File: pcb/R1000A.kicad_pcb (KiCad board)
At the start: 2 copper layers, 106 x 104 mm, 21 parts, among them J1 PCIESOCKET-X1, J10 PCIESOCKET-X1, J11 PCIESOCKET-X1, J12 PCIESOCKET-X1, J13 PCIESOCKET-X1, J14 PCIESOCKET-X1, J2 PCIESOCKET-X1, J3 PCIESOCKET-X1, J4 PCIESOCKET-X1, J5 PCIESOCKET-X1, J6 PCIESOCKET-X1, J7 PCIESOCKET-X1, J8 PCIESOCKET-X1, J9 PCIESOCKET-X1

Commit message: wip
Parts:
- added MP1: RPi_Mount, Main:DOCK_RPI, F.Cu at (102.5, 68.0)
- added U1: LPC1769FBD100,551, Main:QFP050P1400X1400X160-100, F.Cu at (98.8, 68.1)
- J10, J12, J14, J2, J4, J6, J8: moved to F.Cu
- moved J1 51.0 mm to (70.0, 120.0)
- moved J10 51.0 mm to (160.0, 120.0)
- moved J11 51.0 mm to (170.0, 120.0)
- moved J12 51.0 mm to (180.0, 120.0)
- moved J13 51.0 mm to (190.0, 120.0)
- moved J14 51.0 mm to (200.0, 120.0)
- moved J2 51.0 mm to (80.0, 120.0)
- moved J3 51.0 mm to (90.0, 120.0)
- moved J4 51.0 mm to (100.0, 120.0)
- moved J5 51.0 mm to (110.0, 120.0)
- moved J6 51.0 mm to (120.0, 120.0)
- moved J7 51.0 mm to (130.0, 120.0)
- moved J8 51.0 mm to (140.0, 120.0)
- moved J9 51.0 mm to (150.0, 120.0)
- moved R2 29.4 mm to (128.0, 87.4)
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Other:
- board size 106 x 104 mm -> 152 x 104 mm

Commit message: wip
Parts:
- added J15: SOCKET420P-02X04-CPU, Main:SOCKET420P-02X04, F.Cu at (210.0, 120.0)
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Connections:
- J1 pad A1: (no net) -> Net-(J1-PadA1)
- J1 pad A10: (no net) -> Net-(J1-PadA10)
- J1 pad A11: (no net) -> Net-(J1-PadA11)
- J1 pad A12: (no net) -> Net-(J1-PadA12)
- J1 pad A13: (no net) -> Net-(J1-PadA13)
- J1 pad A14: (no net) -> Net-(J1-PadA14)
- J1 pad A15: (no net) -> Net-(J1-PadA15)
- J1 pad A16: (no net) -> Net-(J1-PadA16)
- J1 pad A17: (no net) -> Net-(J1-PadA17)
- J1 pad A18: (no net) -> Net-(J1-PadA18)
- J1 pad A2: (no net) -> Net-(J1-PadA2)
- J1 pad A3: (no net) -> Net-(J1-PadA3)
- J1 pad A4: (no net) -> Net-(J1-PadA4)
- J1 pad A5: (no net) -> Net-(J1-PadA5)
- J1 pad A6: (no net) -> Net-(J1-PadA6)
- J1 pad A7: (no net) -> Net-(J1-PadA7)
- J1 pad A8: (no net) -> Net-(J1-PadA8)
- J1 pad A9: (no net) -> Net-(J1-PadA9)
- J1 pad B1: (no net) -> Net-(J1-PadB1)
- J1 pad B10: (no net) -> Net-(J1-PadB10)
- J1 pad B11: (no net) -> Net-(J1-PadB11)
- J1 pad B12: (no net) -> Net-(J1-PadB12)
- J1 pad B13: (no net) -> Net-(J1-PadB13)
- J1 pad B14: (no net) -> Net-(J1-PadB14)
- J1 pad B15: (no net) -> Net-(J1-PadB15)
- J1 pad B16: (no net) -> Net-(J1-PadB16)
- J1 pad B17: (no net) -> Net-(J1-PadB17)
- J1 pad B18: (no net) -> Net-(J1-PadB18)
- J1 pad B2: (no net) -> Net-(J1-PadB2)
- J1 pad B3: (no net) -> Net-(J1-PadB3)
- J1 pad B4: (no net) -> Net-(J1-PadB4)
- J1 pad B5: (no net) -> Net-(J1-PadB5)
- J1 pad B6: (no net) -> Net-(J1-PadB6)
- J1 pad B7: (no net) -> Net-(J1-PadB7)
- J1 pad B8: (no net) -> Net-(J1-PadB8)
- J1 pad B9: (no net) -> Net-(J1-PadB9)
- J10 pad A1: (no net) -> Net-(J10-PadA1)
- J10 pad A10: (no net) -> Net-(J10-PadA10)
- J10 pad A11: (no net) -> Net-(J10-PadA11)
- J10 pad A12: (no net) -> Net-(J10-PadA12)
- J10 pad A13: (no net) -> Net-(J10-PadA13)
- J10 pad A14: (no net) -> Net-(J10-PadA14)
- J10 pad A15: (no net) -> Net-(J10-PadA15)
- J10 pad A16: (no net) -> Net-(J10-PadA16)
- J10 pad A17: (no net) -> Net-(J10-PadA17)
- J10 pad A18: (no net) -> Net-(J10-PadA18)
- J10 pad A2: (no net) -> Net-(J10-PadA2)
- J10 pad A3: (no net) -> Net-(J10-PadA3)
- J10 pad A4: (no net) -> Net-(J10-PadA4)
- J10 pad A5: (no net) -> Net-(J10-PadA5)
- J10 pad A6: (no net) -> Net-(J10-PadA6)
- J10 pad A7: (no net) -> Net-(J10-PadA7)
- J10 pad A8: (no net) -> Net-(J10-PadA8)
- J10 pad A9: (no net) -> Net-(J10-PadA9)
- J10 pad B1: (no net) -> Net-(J10-PadB1)
- J10 pad B10: (no net) -> Net-(J10-PadB10)
- J10 pad B11: (no net) -> Net-(J10-PadB11)
- J10 pad B12: (no net) -> Net-(J10-PadB12)
- J10 pad B13: (no net) -> Net-(J10-PadB13)
- J10 pad B14: (no net) -> Net-(J10-PadB14)
- J10 pad B15: (no net) -> Net-(J10-PadB15)
- J10 pad B16: (no net) -> Net-(J10-PadB16)
- J10 pad B17: (no net) -> Net-(J10-PadB17)
- J10 pad B18: (no net) -> Net-(J10-PadB18)
- J10 pad B2: (no net) -> Net-(J10-PadB2)
- J10 pad B3: (no net) -> Net-(J10-PadB3)
- J10 pad B4: (no net) -> Net-(J10-PadB4)
- J10 pad B5: (no net) -> Net-(J10-PadB5)
- J10 pad B6: (no net) -> Net-(J10-PadB6)
- J10 pad B7: (no net) -> Net-(J10-PadB7)
- J10 pad B8: (no net) -> Net-(J10-PadB8)
- J10 pad B9: (no net) -> Net-(J10-PadB9)
- J11 pad A1: (no net) -> Net-(J11-PadA1)
- J11 pad A10: (no net) -> Net-(J11-PadA10)
- J11 pad A11: (no net) -> Net-(J11-PadA11)
- J11 pad A12: (no net) -> Net-(J11-PadA12)
- J11 pad A13: (no net) -> Net-(J11-PadA13)
- J11 pad A14: (no net) -> Net-(J11-PadA14)
- J11 pad A15: (no net) -> Net-(J11-PadA15)
- J11 pad A16: (no net) -> Net-(J11-PadA16)
- J11 pad A17: (no net) -> Net-(J11-PadA17)
- J11 pad A18: (no net) -> Net-(J11-PadA18)
- J11 pad A2: (no net) -> Net-(J11-PadA2)
- J11 pad A3: (no net) -> Net-(J11-PadA3)
- J11 pad A4: (no net) -> Net-(J11-PadA4)
- J11 pad A5: (no net) -> Net-(J11-PadA5)
- J11 pad A6: (no net) -> Net-(J11-PadA6)
- J11 pad A7: (no net) -> Net-(J11-PadA7)
- J11 pad A8: (no net) -> Net-(J11-PadA8)
- J11 pad A9: (no net) -> Net-(J11-PadA9)
- J11 pad B1: (no net) -> Net-(J11-PadB1)
- J11 pad B10: (no net) -> Net-(J11-PadB10)
- J11 pad B11: (no net) -> Net-(J11-PadB11)
- J11 pad B12: (no net) -> Net-(J11-PadB12)
- J11 pad B13: (no net) -> Net-(J11-PadB13)
- J11 pad B14: (no net) -> Net-(J11-PadB14)
- J11 pad B15: (no net) -> Net-(J11-PadB15)
- J11 pad B16: (no net) -> Net-(J11-PadB16)
- J11 pad B17: (no net) -> Net-(J11-PadB17)
- J11 pad B18: (no net) -> Net-(J11-PadB18)
- J11 pad B2: (no net) -> Net-(J11-PadB2)
- J11 pad B3: (no net) -> Net-(J11-PadB3)
- J11 pad B4: (no net) -> Net-(J11-PadB4)
- J11 pad B5: (no net) -> Net-(J11-PadB5)
- J11 pad B6: (no net) -> Net-(J11-PadB6)
- J11 pad B7: (no net) -> Net-(J11-PadB7)
- J11 pad B8: (no net) -> Net-(J11-PadB8)
- J11 pad B9: (no net) -> Net-(J11-PadB9)
- J12 pad A1: (no net) -> Net-(J12-PadA1)
- J12 pad A10: (no net) -> Net-(J12-PadA10)
- J12 pad A11: (no net) -> Net-(J12-PadA11)
- J12 pad A12: (no net) -> Net-(J12-PadA12)
- J12 pad A13: (no net) -> Net-(J12-PadA13)
- J12 pad A14: (no net) -> Net-(J12-PadA14)
- J12 pad A15: (no net) -> Net-(J12-PadA15)
- J12 pad A16: (no net) -> Net-(J12-PadA16)
- J12 pad A17: (no net) -> Net-(J12-PadA17)
- J12 pad A18: (no net) -> Net-(J12-PadA18)
- J12 pad A2: (no net) -> Net-(J12-PadA2)
- J12 pad A3: (no net) -> Net-(J12-PadA3)
- J12 pad A4: (no net) -> Net-(J12-PadA4)
- J12 pad A5: (no net) -> Net-(J12-PadA5)
- J12 pad A6: (no net) -> Net-(J12-PadA6)
- J12 pad A7: (no net) -> Net-(J12-PadA7)
- J12 pad A8: (no net) -> Net-(J12-PadA8)
- J12 pad A9: (no net) -> Net-(J12-PadA9)
- J12 pad B1: (no net) -> Net-(J12-PadB1)
- J12 pad B10: (no net) -> Net-(J12-PadB10)
- J12 pad B11: (no net) -> Net-(J12-PadB11)
- J12 pad B12: (no net) -> Net-(J12-PadB12)
- J12 pad B13: (no net) -> Net-(J12-PadB13)
- J12 pad B14: (no net) -> Net-(J12-PadB14)
- J12 pad B15: (no net) -> Net-(J12-PadB15)
- J12 pad B16: (no net) -> Net-(J12-PadB16)
- J12 pad B17: (no net) -> Net-(J12-PadB17)
- J12 pad B18: (no net) -> Net-(J12-PadB18)
- J12 pad B2: (no net) -> Net-(J12-PadB2)
- J12 pad B3: (no net) -> Net-(J12-PadB3)
- J12 pad B4: (no net) -> Net-(J12-PadB4)
- J12 pad B5: (no net) -> Net-(J12-PadB5)
- J12 pad B6: (no net) -> Net-(J12-PadB6)
- J12 pad B7: (no net) -> Net-(J12-PadB7)
- J12 pad B8: (no net) -> Net-(J12-PadB8)
- J12 pad B9: (no net) -> Net-(J12-PadB9)
- J13 pad A1: (no net) -> Net-(J13-PadA1)
- J13 pad A10: (no net) -> Net-(J13-PadA10)
- J13 pad A11: (no net) -> Net-(J13-PadA11)
- J13 pad A12: (no net) -> Net-(J13-PadA12)
- J13 pad A13: (no net) -> Net-(J13-PadA13)
- J13 pad A14: (no net) -> Net-(J13-PadA14)
- J13 pad A15: (no net) -> Net-(J13-PadA15)
- J13 pad A16: (no net) -> Net-(J13-PadA16)
- J13 pad A17: (no net) -> Net-(J13-PadA17)
- J13 pad A18: (no net) -> Net-(J13-PadA18)
- J13 pad A2: (no net) -> Net-(J13-PadA2)
- J13 pad A3: (no net) -> Net-(J13-PadA3)
- J13 pad A4: (no net) -> Net-(J13-PadA4)
- J13 pad A5: (no net) -> Net-(J13-PadA5)
- J13 pad A6: (no net) -> Net-(J13-PadA6)
- J13 pad A7: (no net) -> Net-(J13-PadA7)
- J13 pad A8: (no net) -> Net-(J13-PadA8)
- J13 pad A9: (no net) -> Net-(J13-PadA9)
- J13 pad B1: (no net) -> Net-(J13-PadB1)
- J13 pad B10: (no net) -> Net-(J13-PadB10)
- J13 pad B11: (no net) -> Net-(J13-PadB11)
- J13 pad B12: (no net) -> Net-(J13-PadB12)
- J13 pad B13: (no net) -> Net-(J13-PadB13)
- J13 pad B14: (no net) -> Net-(J13-PadB14)
- J13 pad B15: (no net) -> Net-(J13-PadB15)
- J13 pad B16: (no net) -> Net-(J13-PadB16)
- J13 pad B17: (no net) -> Net-(J13-PadB17)
- J13 pad B18: (no net) -> Net-(J13-PadB18)
- J13 pad B2: (no net) -> Net-(J13-PadB2)
- J13 pad B3: (no net) -> Net-(J13-PadB3)
- J13 pad B4: (no net) -> Net-(J13-PadB4)
- J13 pad B5: (no net) -> Net-(J13-PadB5)
- J13 pad B6: (no net) -> Net-(J13-PadB6)
- J13 pad B7: (no net) -> Net-(J13-PadB7)
- J13 pad B8: (no net) -> Net-(J13-PadB8)
- J13 pad B9: (no net) -> Net-(J13-PadB9)
- J14 pad A1: (no net) -> Net-(J14-PadA1)
- J14 pad A10: (no net) -> Net-(J14-PadA10)
- J14 pad A11: (no net) -> Net-(J14-PadA11)
- J14 pad A12: (no net) -> Net-(J14-PadA12)
- J14 pad A13: (no net) -> Net-(J14-PadA13)
- J14 pad A14: (no net) -> Net-(J14-PadA14)
- J14 pad A15: (no net) -> Net-(J14-PadA15)
- J14 pad A16: (no net) -> Net-(J14-PadA16)
- J14 pad A17: (no net) -> Net-(J14-PadA17)
- J14 pad A18: (no net) -> Net-(J14-PadA18)
- J14 pad A2: (no net) -> Net-(J14-PadA2)
- J14 pad A3: (no net) -> Net-(J14-PadA3)
- J14 pad A4: (no net) -> Net-(J14-PadA4)
- J14 pad A5: (no net) -> Net-(J14-PadA5)
- J14 pad A6: (no net) -> Net-(J14-PadA6)
- J14 pad A7: (no net) -> Net-(J14-PadA7)
- J14 pad A8: (no net) -> Net-(J14-PadA8)
- J14 pad A9: (no net) -> Net-(J14-PadA9)
- J14 pad B1: (no net) -> Net-(J14-PadB1)
- J14 pad B10: (no net) -> Net-(J14-PadB10)
- J14 pad B11: (no net) -> Net-(J14-PadB11)
- J14 pad B12: (no net) -> Net-(J14-PadB12)
- J14 pad B13: (no net) -> Net-(J14-PadB13)
- J14 pad B14: (no net) -> Net-(J14-PadB14)
- J14 pad B15: (no net) -> Net-(J14-PadB15)
- J14 pad B16: (no net) -> Net-(J14-PadB16)
- J14 pad B17: (no net) -> Net-(J14-PadB17)
- J14 pad B18: (no net) -> Net-(J14-PadB18)
- J14 pad B2: (no net) -> Net-(J14-PadB2)
- J14 pad B3: (no net) -> Net-(J14-PadB3)
- J14 pad B4: (no net) -> Net-(J14-PadB4)
- J14 pad B5: (no net) -> Net-(J14-PadB5)
- J14 pad B6: (no net) -> Net-(J14-PadB6)
- J14 pad B7: (no net) -> Net-(J14-PadB7)
- J14 pad B8: (no net) -> Net-(J14-PadB8)
- J14 pad B9: (no net) -> Net-(J14-PadB9)
- J2 pad A1: (no net) -> Net-(J2-PadA1)
- J2 pad A10: (no net) -> Net-(J2-PadA10)
- J2 pad A11: (no net) -> Net-(J2-PadA11)
- J2 pad A12: (no net) -> Net-(J2-PadA12)
- J2 pad A13: (no net) -> Net-(J2-PadA13)
- J2 pad A14: (no net) -> Net-(J2-PadA14)
- J2 pad A15: (no net) -> Net-(J2-PadA15)
- J2 pad A16: (no net) -> Net-(J2-PadA16)
- J2 pad A17: (no net) -> Net-(J2-PadA17)
- J2 pad A18: (no net) -> Net-(J2-PadA18)
- J2 pad A2: (no net) -> Net-(J2-PadA2)
- J2 pad A3: (no net) -> Net-(J2-PadA3)
- J2 pad A4: (no net) -> Net-(J2-PadA4)
- J2 pad A5: (no net) -> Net-(J2-PadA5)
- J2 pad A6: (no net) -> Net-(J2-PadA6)
- J2 pad A7: (no net) -> Net-(J2-PadA7)
- J2 pad A8: (no net) -> Net-(J2-PadA8)
- J2 pad A9: (no net) -> Net-(J2-PadA9)
- J2 pad B1: (no net) -> Net-(J2-PadB1)
- J2 pad B10: (no net) -> Net-(J2-PadB10)
- J2 pad B11: (no net) -> Net-(J2-PadB11)
- J2 pad B12: (no net) -> Net-(J2-PadB12)
- J2 pad B13: (no net) -> Net-(J2-PadB13)
- J2 pad B14: (no net) -> Net-(J2-PadB14)
- J2 pad B15: (no net) -> Net-(J2-PadB15)
- J2 pad B16: (no net) -> Net-(J2-PadB16)
- J2 pad B17: (no net) -> Net-(J2-PadB17)
- J2 pad B18: (no net) -> Net-(J2-PadB18)
- J2 pad B2: (no net) -> Net-(J2-PadB2)
- J2 pad B3: (no net) -> Net-(J2-PadB3)
- J2 pad B4: (no net) -> Net-(J2-PadB4)
- J2 pad B5: (no net) -> Net-(J2-PadB5)
- J2 pad B6: (no net) -> Net-(J2-PadB6)
- J2 pad B7: (no net) -> Net-(J2-PadB7)
- J2 pad B8: (no net) -> Net-(J2-PadB8)
- J2 pad B9: (no net) -> Net-(J2-PadB9)
- J3 pad A1: (no net) -> Net-(J3-PadA1)
- J3 pad A10: (no net) -> Net-(J3-PadA10)
- J3 pad A11: (no net) -> Net-(J3-PadA11)
- J3 pad A12: (no net) -> Net-(J3-PadA12)
- J3 pad A13: (no net) -> Net-(J3-PadA13)
- J3 pad A14: (no net) -> Net-(J3-PadA14)
- J3 pad A15: (no net) -> Net-(J3-PadA15)
- J3 pad A16: (no net) -> Net-(J3-PadA16)
- J3 pad A17: (no net) -> Net-(J3-PadA17)
- J3 pad A18: (no net) -> Net-(J3-PadA18)
- J3 pad A2: (no net) -> Net-(J3-PadA2)
- J3 pad A3: (no net) -> Net-(J3-PadA3)
- J3 pad A4: (no net) -> Net-(J3-PadA4)
- J3 pad A5: (no net) -> Net-(J3-PadA5)
- J3 pad A6: (no net) -> Net-(J3-PadA6)
- J3 pad A7: (no net) -> Net-(J3-PadA7)
- J3 pad A8: (no net) -> Net-(J3-PadA8)
- J3 pad A9: (no net) -> Net-(J3-PadA9)
- J3 pad B1: (no net) -> Net-(J3-PadB1)
- J3 pad B10: (no net) -> Net-(J3-PadB10)
- J3 pad B11: (no net) -> Net-(J3-PadB11)
- J3 pad B12: (no net) -> Net-(J3-PadB12)
- J3 pad B13: (no net) -> Net-(J3-PadB13)
- J3 pad B14: (no net) -> Net-(J3-PadB14)
- J3 pad B15: (no net) -> Net-(J3-PadB15)
- J3 pad B16: (no net) -> Net-(J3-PadB16)
- J3 pad B17: (no net) -> Net-(J3-PadB17)
- J3 pad B18: (no net) -> Net-(J3-PadB18)
- J3 pad B2: (no net) -> Net-(J3-PadB2)
- J3 pad B3: (no net) -> Net-(J3-PadB3)
- J3 pad B4: (no net) -> Net-(J3-PadB4)
- J3 pad B5: (no net) -> Net-(J3-PadB5)
- J3 pad B6: (no net) -> Net-(J3-PadB6)
- J3 pad B7: (no net) -> Net-(J3-PadB7)
- J3 pad B8: (no net) -> Net-(J3-PadB8)
- J3 pad B9: (no net) -> Net-(J3-PadB9)
- J4 pad A1: (no net) -> Net-(J4-PadA1)
- J4 pad A10: (no net) -> Net-(J4-PadA10)
- J4 pad A11: (no net) -> Net-(J4-PadA11)
- J4 pad A12: (no net) -> Net-(J4-PadA12)
- J4 pad A13: (no net) -> Net-(J4-PadA13)
- J4 pad A14: (no net) -> Net-(J4-PadA14)
- J4 pad A15: (no net) -> Net-(J4-PadA15)
- J4 pad A16: (no net) -> Net-(J4-PadA16)
- J4 pad A17: (no net) -> Net-(J4-PadA17)
- J4 pad A18: (no net) -> Net-(J4-PadA18)
- J4 pad A2: (no net) -> Net-(J4-PadA2)
- J4 pad A3: (no net) -> Net-(J4-PadA3)
- J4 pad A4: (no net) -> Net-(J4-PadA4)
- J4 pad A5: (no net) -> Net-(J4-PadA5)
- J4 pad A6: (no net) -> Net-(J4-PadA6)
- J4 pad A7: (no net) -> Net-(J4-PadA7)
- J4 pad A8: (no net) -> Net-(J4-PadA8)
- J4 pad A9: (no net) -> Net-(J4-PadA9)
- J4 pad B1: (no net) -> Net-(J4-PadB1)
- J4 pad B10: (no net) -> Net-(J4-PadB10)
- J4 pad B11: (no net) -> Net-(J4-PadB11)
- J4 pad B12: (no net) -> Net-(J4-PadB12)
- J4 pad B13: (no net) -> Net-(J4-PadB13)
- J4 pad B14: (no net) -> Net-(J4-PadB14)
- J4 pad B15: (no net) -> Net-(J4-PadB15)
- J4 pad B16: (no net) -> Net-(J4-PadB16)
- J4 pad B17: (no net) -> Net-(J4-PadB17)
- J4 pad B18: (no net) -> Net-(J4-PadB18)
- J4 pad B2: (no net) -> Net-(J4-PadB2)
- J4 pad B3: (no net) -> Net-(J4-PadB3)
- J4 pad B4: (no net) -> Net-(J4-PadB4)
- J4 pad B5: (no net) -> Net-(J4-PadB5)
- J4 pad B6: (no net) -> Net-(J4-PadB6)
- J4 pad B7: (no net) -> Net-(J4-PadB7)
- J4 pad B8: (no net) -> Net-(J4-PadB8)
- J4 pad B9: (no net) -> Net-(J4-PadB9)
- J5 pad A1: (no net) -> Net-(J5-PadA1)
- J5 pad A10: (no net) -> Net-(J5-PadA10)
- J5 pad A11: (no net) -> Net-(J5-PadA11)
- J5 pad A12: (no net) -> Net-(J5-PadA12)
- J5 pad A13: (no net) -> Net-(J5-PadA13)
- J5 pad A14: (no net) -> Net-(J5-PadA14)
- J5 pad A15: (no net) -> Net-(J5-PadA15)
- J5 pad A16: (no net) -> Net-(J5-PadA16)
- J5 pad A17: (no net) -> Net-(J5-PadA17)
- J5 pad A18: (no net) -> Net-(J5-PadA18)
- J5 pad A2: (no net) -> Net-(J5-PadA2)
- J5 pad A3: (no net) -> Net-(J5-PadA3)
- J5 pad A4: (no net) -> Net-(J5-PadA4)
- J5 pad A5: (no net) -> Net-(J5-PadA5)
- J5 pad A6: (no net) -> Net-(J5-PadA6)
- J5 pad A7: (no net) -> Net-(J5-PadA7)
- J5 pad A8: (no net) -> Net-(J5-PadA8)
- J5 pad A9: (no net) -> Net-(J5-PadA9)
- J5 pad B1: (no net) -> Net-(J5-PadB1)
- J5 pad B10: (no net) -> Net-(J5-PadB10)
- J5 pad B11: (no net) -> Net-(J5-PadB11)
- J5 pad B12: (no net) -> Net-(J5-PadB12)
- J5 pad B13: (no net) -> Net-(J5-PadB13)
- J5 pad B14: (no net) -> Net-(J5-PadB14)
- J5 pad B15: (no net) -> Net-(J5-PadB15)
- J5 pad B16: (no net) -> Net-(J5-PadB16)
- J5 pad B17: (no net) -> Net-(J5-PadB17)
- J5 pad B18: (no net) -> Net-(J5-PadB18)
- J5 pad B2: (no net) -> Net-(J5-PadB2)
- J5 pad B3: (no net) -> Net-(J5-PadB3)
- J5 pad B4: (no net) -> Net-(J5-PadB4)
- J5 pad B5: (no net) -> Net-(J5-PadB5)
- J5 pad B6: (no net) -> Net-(J5-PadB6)
- J5 pad B7: (no net) -> Net-(J5-PadB7)
- J5 pad B8: (no net) -> Net-(J5-PadB8)
- J5 pad B9: (no net) -> Net-(J5-PadB9)
- J6 pad A1: (no net) -> Net-(J6-PadA1)
- J6 pad A10: (no net) -> Net-(J6-PadA10)
- J6 pad A11: (no net) -> Net-(J6-PadA11)
- J6 pad A12: (no net) -> Net-(J6-PadA12)
- J6 pad A13: (no net) -> Net-(J6-PadA13)
- J6 pad A14: (no net) -> Net-(J6-PadA14)
- J6 pad A15: (no net) -> Net-(J6-PadA15)
- J6 pad A16: (no net) -> Net-(J6-PadA16)
- J6 pad A17: (no net) -> Net-(J6-PadA17)
- J6 pad A18: (no net) -> Net-(J6-PadA18)
- J6 pad A2: (no net) -> Net-(J6-PadA2)
- J6 pad A3: (no net) -> Net-(J6-PadA3)
- J6 pad A4: (no net) -> Net-(J6-PadA4)
- J6 pad A5: (no net) -> Net-(J6-PadA5)
- J6 pad A6: (no net) -> Net-(J6-PadA6)
- J6 pad A7: (no net) -> Net-(J6-PadA7)
- J6 pad A8: (no net) -> Net-(J6-PadA8)
- J6 pad A9: (no net) -> Net-(J6-PadA9)
- J6 pad B1: (no net) -> Net-(J6-PadB1)
- J6 pad B10: (no net) -> Net-(J6-PadB10)
- J6 pad B11: (no net) -> Net-(J6-PadB11)
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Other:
- board size 152 x 104 mm -> 162 x 104 mm

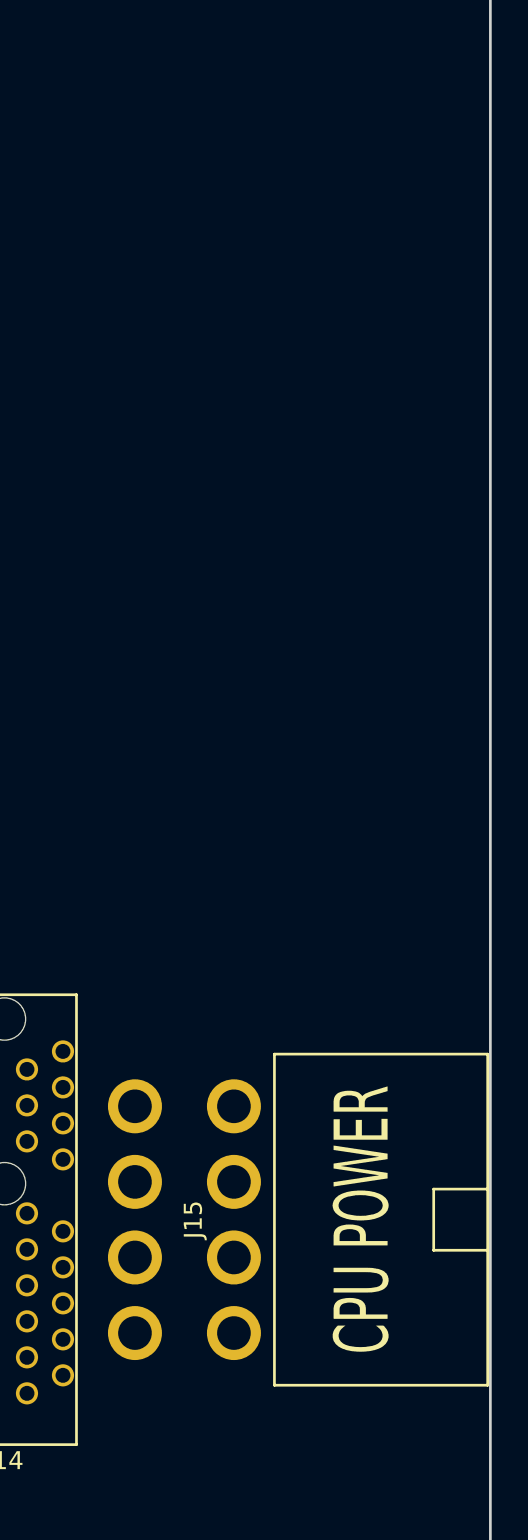
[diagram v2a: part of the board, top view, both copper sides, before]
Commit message: added 4 pin board to wire
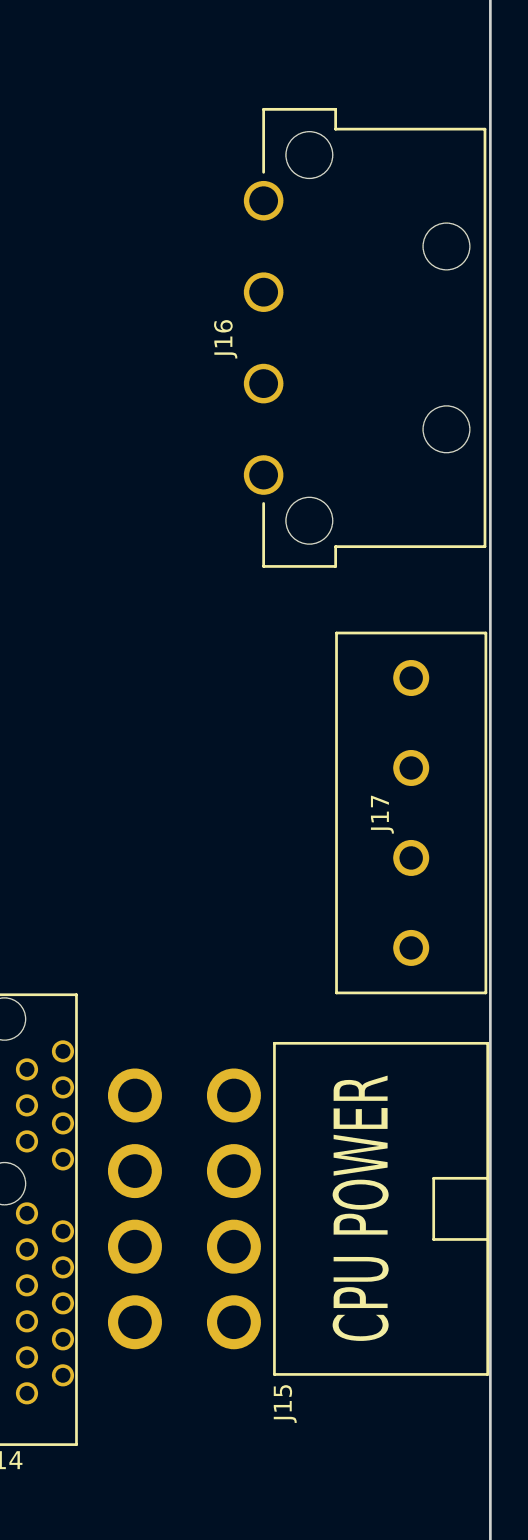
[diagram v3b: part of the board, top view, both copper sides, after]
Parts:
- added J16: SOCKET508P-01X04, Main:SOCKET508P-01X04, F.Cu at (214.4, 71.0)
- added J17: CONN500P-01X04, Main:CONN500P-01X04, F.Cu at (222.6, 97.4)
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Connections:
- J1 pad A1: Net-(J1-PadA1) -> (no net)
- J1 pad A10: Net-(J1-PadA10) -> (no net)
- J1 pad A11: Net-(J1-PadA11) -> (no net)
- J1 pad A12: Net-(J1-PadA12) -> (no net)
- J1 pad A13: Net-(J1-PadA13) -> (no net)
- J1 pad A14: Net-(J1-PadA14) -> (no net)
- J1 pad A15: Net-(J1-PadA15) -> (no net)
- J1 pad A16: Net-(J1-PadA16) -> (no net)
- J1 pad A17: Net-(J1-PadA17) -> (no net)
- J1 pad A18: Net-(J1-PadA18) -> (no net)
- J1 pad A2: Net-(J1-PadA2) -> (no net)
- J1 pad A3: Net-(J1-PadA3) -> (no net)
- J1 pad A4: Net-(J1-PadA4) -> (no net)
- J1 pad A5: Net-(J1-PadA5) -> (no net)
- J1 pad A6: Net-(J1-PadA6) -> (no net)
- J1 pad A7: Net-(J1-PadA7) -> (no net)
- J1 pad A8: Net-(J1-PadA8) -> (no net)
- J1 pad A9: Net-(J1-PadA9) -> (no net)
- J1 pad B1: Net-(J1-PadB1) -> (no net)
- J1 pad B10: Net-(J1-PadB10) -> (no net)
- J1 pad B11: Net-(J1-PadB11) -> (no net)
- J1 pad B12: Net-(J1-PadB12) -> (no net)
- J1 pad B13: Net-(J1-PadB13) -> (no net)
- J1 pad B14: Net-(J1-PadB14) -> (no net)
- J1 pad B15: Net-(J1-PadB15) -> (no net)
- J1 pad B16: Net-(J1-PadB16) -> (no net)
- J1 pad B17: Net-(J1-PadB17) -> (no net)
- J1 pad B18: Net-(J1-PadB18) -> (no net)
- J1 pad B2: Net-(J1-PadB2) -> (no net)
- J1 pad B3: Net-(J1-PadB3) -> (no net)
- J1 pad B4: Net-(J1-PadB4) -> (no net)
- J1 pad B5: Net-(J1-PadB5) -> (no net)
- J1 pad B6: Net-(J1-PadB6) -> (no net)
- J1 pad B7: Net-(J1-PadB7) -> (no net)
- J1 pad B8: Net-(J1-PadB8) -> (no net)
- J1 pad B9: Net-(J1-PadB9) -> (no net)
- J10 pad A1: Net-(J10-PadA1) -> (no net)
- J10 pad A10: Net-(J10-PadA10) -> (no net)
- J10 pad A11: Net-(J10-PadA11) -> (no net)
- J10 pad A12: Net-(J10-PadA12) -> (no net)
- J10 pad A13: Net-(J10-PadA13) -> (no net)
- J10 pad A14: Net-(J10-PadA14) -> (no net)
- J10 pad A15: Net-(J10-PadA15) -> (no net)
- J10 pad A16: Net-(J10-PadA16) -> (no net)
- J10 pad A17: Net-(J10-PadA17) -> (no net)
- J10 pad A18: Net-(J10-PadA18) -> (no net)
- J10 pad A2: Net-(J10-PadA2) -> (no net)
- J10 pad A3: Net-(J10-PadA3) -> (no net)
- J10 pad A4: Net-(J10-PadA4) -> (no net)
- J10 pad A5: Net-(J10-PadA5) -> (no net)
- J10 pad A6: Net-(J10-PadA6) -> (no net)
- J10 pad A7: Net-(J10-PadA7) -> (no net)
- J10 pad A8: Net-(J10-PadA8) -> (no net)
- J10 pad A9: Net-(J10-PadA9) -> (no net)
- J10 pad B1: Net-(J10-PadB1) -> (no net)
- J10 pad B10: Net-(J10-PadB10) -> (no net)
- J10 pad B11: Net-(J10-PadB11) -> (no net)
- J10 pad B12: Net-(J10-PadB12) -> (no net)
- J10 pad B13: Net-(J10-PadB13) -> (no net)
- J10 pad B14: Net-(J10-PadB14) -> (no net)
- J10 pad B15: Net-(J10-PadB15) -> (no net)
- J10 pad B16: Net-(J10-PadB16) -> (no net)
- J10 pad B17: Net-(J10-PadB17) -> (no net)
- J10 pad B18: Net-(J10-PadB18) -> (no net)
- J10 pad B2: Net-(J10-PadB2) -> (no net)
- J10 pad B3: Net-(J10-PadB3) -> (no net)
- J10 pad B4: Net-(J10-PadB4) -> (no net)
- J10 pad B5: Net-(J10-PadB5) -> (no net)
- J10 pad B6: Net-(J10-PadB6) -> (no net)
- J10 pad B7: Net-(J10-PadB7) -> (no net)
- J10 pad B8: Net-(J10-PadB8) -> (no net)
- J10 pad B9: Net-(J10-PadB9) -> (no net)
- J11 pad A1: Net-(J11-PadA1) -> (no net)
- J11 pad A10: Net-(J11-PadA10) -> (no net)
- J11 pad A11: Net-(J11-PadA11) -> (no net)
- J11 pad A12: Net-(J11-PadA12) -> (no net)
- J11 pad A13: Net-(J11-PadA13) -> (no net)
- J11 pad A14: Net-(J11-PadA14) -> (no net)
- J11 pad A15: Net-(J11-PadA15) -> (no net)
- J11 pad A16: Net-(J11-PadA16) -> (no net)
- J11 pad A17: Net-(J11-PadA17) -> (no net)
- J11 pad A18: Net-(J11-PadA18) -> (no net)
- J11 pad A2: Net-(J11-PadA2) -> (no net)
- J11 pad A3: Net-(J11-PadA3) -> (no net)
- J11 pad A4: Net-(J11-PadA4) -> (no net)
- J11 pad A5: Net-(J11-PadA5) -> (no net)
- J11 pad A6: Net-(J11-PadA6) -> (no net)
- J11 pad A7: Net-(J11-PadA7) -> (no net)
- J11 pad A8: Net-(J11-PadA8) -> (no net)
- J11 pad A9: Net-(J11-PadA9) -> (no net)
- J11 pad B1: Net-(J11-PadB1) -> (no net)
- J11 pad B10: Net-(J11-PadB10) -> (no net)
- J11 pad B11: Net-(J11-PadB11) -> (no net)
- J11 pad B12: Net-(J11-PadB12) -> (no net)
- J11 pad B13: Net-(J11-PadB13) -> (no net)
- J11 pad B14: Net-(J11-PadB14) -> (no net)
- J11 pad B15: Net-(J11-PadB15) -> (no net)
- J11 pad B16: Net-(J11-PadB16) -> (no net)
- J11 pad B17: Net-(J11-PadB17) -> (no net)
- J11 pad B18: Net-(J11-PadB18) -> (no net)
- J11 pad B2: Net-(J11-PadB2) -> (no net)
- J11 pad B3: Net-(J11-PadB3) -> (no net)
- J11 pad B4: Net-(J11-PadB4) -> (no net)
- J11 pad B5: Net-(J11-PadB5) -> (no net)
- J11 pad B6: Net-(J11-PadB6) -> (no net)
- J11 pad B7: Net-(J11-PadB7) -> (no net)
- J11 pad B8: Net-(J11-PadB8) -> (no net)
- J11 pad B9: Net-(J11-PadB9) -> (no net)
- J12 pad A1: Net-(J12-PadA1) -> (no net)
- J12 pad A10: Net-(J12-PadA10) -> (no net)
- J12 pad A11: Net-(J12-PadA11) -> (no net)
- J12 pad A12: Net-(J12-PadA12) -> (no net)
- J12 pad A13: Net-(J12-PadA13) -> (no net)
- J12 pad A14: Net-(J12-PadA14) -> (no net)
- J12 pad A15: Net-(J12-PadA15) -> (no net)
- J12 pad A16: Net-(J12-PadA16) -> (no net)
- J12 pad A17: Net-(J12-PadA17) -> (no net)
- J12 pad A18: Net-(J12-PadA18) -> (no net)
- J12 pad A2: Net-(J12-PadA2) -> (no net)
- J12 pad A3: Net-(J12-PadA3) -> (no net)
- J12 pad A4: Net-(J12-PadA4) -> (no net)
- J12 pad A5: Net-(J12-PadA5) -> (no net)
- J12 pad A6: Net-(J12-PadA6) -> (no net)
- J12 pad A7: Net-(J12-PadA7) -> (no net)
- J12 pad A8: Net-(J12-PadA8) -> (no net)
- J12 pad A9: Net-(J12-PadA9) -> (no net)
- J12 pad B1: Net-(J12-PadB1) -> (no net)
- J12 pad B10: Net-(J12-PadB10) -> (no net)
- J12 pad B11: Net-(J12-PadB11) -> (no net)
- J12 pad B12: Net-(J12-PadB12) -> (no net)
- J12 pad B13: Net-(J12-PadB13) -> (no net)
- J12 pad B14: Net-(J12-PadB14) -> (no net)
- J12 pad B15: Net-(J12-PadB15) -> (no net)
- J12 pad B16: Net-(J12-PadB16) -> (no net)
- J12 pad B17: Net-(J12-PadB17) -> (no net)
- J12 pad B18: Net-(J12-PadB18) -> (no net)
- J12 pad B2: Net-(J12-PadB2) -> (no net)
- J12 pad B3: Net-(J12-PadB3) -> (no net)
- J12 pad B4: Net-(J12-PadB4) -> (no net)
- J12 pad B5: Net-(J12-PadB5) -> (no net)
- J12 pad B6: Net-(J12-PadB6) -> (no net)
- J12 pad B7: Net-(J12-PadB7) -> (no net)
- J12 pad B8: Net-(J12-PadB8) -> (no net)
- J12 pad B9: Net-(J12-PadB9) -> (no net)
- J13 pad A1: Net-(J13-PadA1) -> (no net)
- J13 pad A10: Net-(J13-PadA10) -> (no net)
- J13 pad A11: Net-(J13-PadA11) -> (no net)
- J13 pad A12: Net-(J13-PadA12) -> (no net)
- J13 pad A13: Net-(J13-PadA13) -> (no net)
- J13 pad A14: Net-(J13-PadA14) -> (no net)
- J13 pad A15: Net-(J13-PadA15) -> (no net)
- J13 pad A16: Net-(J13-PadA16) -> (no net)
- J13 pad A17: Net-(J13-PadA17) -> (no net)
- J13 pad A18: Net-(J13-PadA18) -> (no net)
- J13 pad A2: Net-(J13-PadA2) -> (no net)
- J13 pad A3: Net-(J13-PadA3) -> (no net)
- J13 pad A4: Net-(J13-PadA4) -> (no net)
- J13 pad A5: Net-(J13-PadA5) -> (no net)
- J13 pad A6: Net-(J13-PadA6) -> (no net)
- J13 pad A7: Net-(J13-PadA7) -> (no net)
- J13 pad A8: Net-(J13-PadA8) -> (no net)
- J13 pad A9: Net-(J13-PadA9) -> (no net)
- J13 pad B1: Net-(J13-PadB1) -> (no net)
- J13 pad B10: Net-(J13-PadB10) -> (no net)
- J13 pad B11: Net-(J13-PadB11) -> (no net)
- J13 pad B12: Net-(J13-PadB12) -> (no net)
- J13 pad B13: Net-(J13-PadB13) -> (no net)
- J13 pad B14: Net-(J13-PadB14) -> (no net)
- J13 pad B15: Net-(J13-PadB15) -> (no net)
- J13 pad B16: Net-(J13-PadB16) -> (no net)
- J13 pad B17: Net-(J13-PadB17) -> (no net)
- J13 pad B18: Net-(J13-PadB18) -> (no net)
- J13 pad B2: Net-(J13-PadB2) -> (no net)
- J13 pad B3: Net-(J13-PadB3) -> (no net)
- J13 pad B4: Net-(J13-PadB4) -> (no net)
- J13 pad B5: Net-(J13-PadB5) -> (no net)
- J13 pad B6: Net-(J13-PadB6) -> (no net)
- J13 pad B7: Net-(J13-PadB7) -> (no net)
- J13 pad B8: Net-(J13-PadB8) -> (no net)
- J13 pad B9: Net-(J13-PadB9) -> (no net)
- J14 pad A1: Net-(J14-PadA1) -> (no net)
- J14 pad A10: Net-(J14-PadA10) -> (no net)
- J14 pad A11: Net-(J14-PadA11) -> (no net)
- J14 pad A12: Net-(J14-PadA12) -> (no net)
- J14 pad A13: Net-(J14-PadA13) -> (no net)
- J14 pad A14: Net-(J14-PadA14) -> (no net)
- J14 pad A15: Net-(J14-PadA15) -> (no net)
- J14 pad A16: Net-(J14-PadA16) -> (no net)
- J14 pad A17: Net-(J14-PadA17) -> (no net)
- J14 pad A18: Net-(J14-PadA18) -> (no net)
- J14 pad A2: Net-(J14-PadA2) -> (no net)
- J14 pad A3: Net-(J14-PadA3) -> (no net)
- J14 pad A4: Net-(J14-PadA4) -> (no net)
- J14 pad A5: Net-(J14-PadA5) -> (no net)
- J14 pad A6: Net-(J14-PadA6) -> (no net)
- J14 pad A7: Net-(J14-PadA7) -> (no net)
- J14 pad A8: Net-(J14-PadA8) -> (no net)
- J14 pad A9: Net-(J14-PadA9) -> (no net)
- J14 pad B1: Net-(J14-PadB1) -> (no net)
- J14 pad B10: Net-(J14-PadB10) -> (no net)
- J14 pad B11: Net-(J14-PadB11) -> (no net)
- J14 pad B12: Net-(J14-PadB12) -> (no net)
- J14 pad B13: Net-(J14-PadB13) -> (no net)
- J14 pad B14: Net-(J14-PadB14) -> (no net)
- J14 pad B15: Net-(J14-PadB15) -> (no net)
- J14 pad B16: Net-(J14-PadB16) -> (no net)
- J14 pad B17: Net-(J14-PadB17) -> (no net)
- J14 pad B18: Net-(J14-PadB18) -> (no net)
- J14 pad B2: Net-(J14-PadB2) -> (no net)
- J14 pad B3: Net-(J14-PadB3) -> (no net)
- J14 pad B4: Net-(J14-PadB4) -> (no net)
- J14 pad B5: Net-(J14-PadB5) -> (no net)
- J14 pad B6: Net-(J14-PadB6) -> (no net)
- J14 pad B7: Net-(J14-PadB7) -> (no net)
- J14 pad B8: Net-(J14-PadB8) -> (no net)
- J14 pad B9: Net-(J14-PadB9) -> (no net)
- J15 pad 1: Net-(J15-Pad1) -> (no net)
- J15 pad 2: Net-(J15-Pad2) -> (no net)
- J15 pad 3: Net-(J15-Pad3) -> (no net)
- J15 pad 4: Net-(J15-Pad4) -> (no net)
- J15 pad 5: Net-(J15-Pad5) -> (no net)
- J15 pad 6: Net-(J15-Pad6) -> (no net)
- J15 pad 7: Net-(J15-Pad7) -> (no net)
- J15 pad 8: Net-(J15-Pad8) -> (no net)
- J2 pad A1: Net-(J2-PadA1) -> (no net)
- J2 pad A10: Net-(J2-PadA10) -> (no net)
- J2 pad A11: Net-(J2-PadA11) -> (no net)
- J2 pad A12: Net-(J2-PadA12) -> (no net)
- J2 pad A13: Net-(J2-PadA13) -> (no net)
- J2 pad A14: Net-(J2-PadA14) -> (no net)
- J2 pad A15: Net-(J2-PadA15) -> (no net)
- J2 pad A16: Net-(J2-PadA16) -> (no net)
- J2 pad A17: Net-(J2-PadA17) -> (no net)
- J2 pad A18: Net-(J2-PadA18) -> (no net)
- J2 pad A2: Net-(J2-PadA2) -> (no net)
- J2 pad A3: Net-(J2-PadA3) -> (no net)
- J2 pad A4: Net-(J2-PadA4) -> (no net)
- J2 pad A5: Net-(J2-PadA5) -> (no net)
- J2 pad A6: Net-(J2-PadA6) -> (no net)
- J2 pad A7: Net-(J2-PadA7) -> (no net)
- J2 pad A8: Net-(J2-PadA8) -> (no net)
- J2 pad A9: Net-(J2-PadA9) -> (no net)
- J2 pad B1: Net-(J2-PadB1) -> (no net)
- J2 pad B10: Net-(J2-PadB10) -> (no net)
- J2 pad B11: Net-(J2-PadB11) -> (no net)
- J2 pad B12: Net-(J2-PadB12) -> (no net)
- J2 pad B13: Net-(J2-PadB13) -> (no net)
- J2 pad B14: Net-(J2-PadB14) -> (no net)
- J2 pad B15: Net-(J2-PadB15) -> (no net)
- J2 pad B16: Net-(J2-PadB16) -> (no net)
- J2 pad B17: Net-(J2-PadB17) -> (no net)
- J2 pad B18: Net-(J2-PadB18) -> (no net)
- J2 pad B2: Net-(J2-PadB2) -> (no net)
- J2 pad B3: Net-(J2-PadB3) -> (no net)
- J2 pad B4: Net-(J2-PadB4) -> (no net)
- J2 pad B5: Net-(J2-PadB5) -> (no net)
- J2 pad B6: Net-(J2-PadB6) -> (no net)
- J2 pad B7: Net-(J2-PadB7) -> (no net)
- J2 pad B8: Net-(J2-PadB8) -> (no net)
- J2 pad B9: Net-(J2-PadB9) -> (no net)
- J3 pad A1: Net-(J3-PadA1) -> (no net)
- J3 pad A10: Net-(J3-PadA10) -> (no net)
- J3 pad A11: Net-(J3-PadA11) -> (no net)
- J3 pad A12: Net-(J3-PadA12) -> (no net)
- J3 pad A13: Net-(J3-PadA13) -> (no net)
- J3 pad A14: Net-(J3-PadA14) -> (no net)
- J3 pad A15: Net-(J3-PadA15) -> (no net)
- J3 pad A16: Net-(J3-PadA16) -> (no net)
- J3 pad A17: Net-(J3-PadA17) -> (no net)
- J3 pad A18: Net-(J3-PadA18) -> (no net)
- J3 pad A2: Net-(J3-PadA2) -> (no net)
- J3 pad A3: Net-(J3-PadA3) -> (no net)
- J3 pad A4: Net-(J3-PadA4) -> (no net)
- J3 pad A5: Net-(J3-PadA5) -> (no net)
- J3 pad A6: Net-(J3-PadA6) -> (no net)
- J3 pad A7: Net-(J3-PadA7) -> (no net)
- J3 pad A8: Net-(J3-PadA8) -> (no net)
- J3 pad A9: Net-(J3-PadA9) -> (no net)
- J3 pad B1: Net-(J3-PadB1) -> (no net)
- J3 pad B10: Net-(J3-PadB10) -> (no net)
- J3 pad B11: Net-(J3-PadB11) -> (no net)
- J3 pad B12: Net-(J3-PadB12) -> (no net)
- J3 pad B13: Net-(J3-PadB13) -> (no net)
- J3 pad B14: Net-(J3-PadB14) -> (no net)
- J3 pad B15: Net-(J3-PadB15) -> (no net)
- J3 pad B16: Net-(J3-PadB16) -> (no net)
- J3 pad B17: Net-(J3-PadB17) -> (no net)
- J3 pad B18: Net-(J3-PadB18) -> (no net)
- J3 pad B2: Net-(J3-PadB2) -> (no net)
- J3 pad B3: Net-(J3-PadB3) -> (no net)
- J3 pad B4: Net-(J3-PadB4) -> (no net)
- J3 pad B5: Net-(J3-PadB5) -> (no net)
- J3 pad B6: Net-(J3-PadB6) -> (no net)
- J3 pad B7: Net-(J3-PadB7) -> (no net)
- J3 pad B8: Net-(J3-PadB8) -> (no net)
- J3 pad B9: Net-(J3-PadB9) -> (no net)
- J4 pad A1: Net-(J4-PadA1) -> (no net)
- J4 pad A10: Net-(J4-PadA10) -> (no net)
- J4 pad A11: Net-(J4-PadA11) -> (no net)
- J4 pad A12: Net-(J4-PadA12) -> (no net)
- J4 pad A13: Net-(J4-PadA13) -> (no net)
- J4 pad A14: Net-(J4-PadA14) -> (no net)
- J4 pad A15: Net-(J4-PadA15) -> (no net)
- J4 pad A16: Net-(J4-PadA16) -> (no net)
- J4 pad A17: Net-(J4-PadA17) -> (no net)
- J4 pad A18: Net-(J4-PadA18) -> (no net)
- J4 pad A2: Net-(J4-PadA2) -> (no net)
- J4 pad A3: Net-(J4-PadA3) -> (no net)
- J4 pad A4: Net-(J4-PadA4) -> (no net)
- J4 pad A5: Net-(J4-PadA5) -> (no net)
- J4 pad A6: Net-(J4-PadA6) -> (no net)
- J4 pad A7: Net-(J4-PadA7) -> (no net)
- J4 pad A8: Net-(J4-PadA8) -> (no net)
- J4 pad A9: Net-(J4-PadA9) -> (no net)
- J4 pad B1: Net-(J4-PadB1) -> (no net)
- J4 pad B10: Net-(J4-PadB10) -> (no net)
- J4 pad B11: Net-(J4-PadB11) -> (no net)
- J4 pad B12: Net-(J4-PadB12) -> (no net)
- J4 pad B13: Net-(J4-PadB13) -> (no net)
- J4 pad B14: Net-(J4-PadB14) -> (no net)
- J4 pad B15: Net-(J4-PadB15) -> (no net)
- J4 pad B16: Net-(J4-PadB16) -> (no net)
- J4 pad B17: Net-(J4-PadB17) -> (no net)
- J4 pad B18: Net-(J4-PadB18) -> (no net)
- J4 pad B2: Net-(J4-PadB2) -> (no net)
- J4 pad B3: Net-(J4-PadB3) -> (no net)
- J4 pad B4: Net-(J4-PadB4) -> (no net)
- J4 pad B5: Net-(J4-PadB5) -> (no net)
- J4 pad B6: Net-(J4-PadB6) -> (no net)
- J4 pad B7: Net-(J4-PadB7) -> (no net)
- J4 pad B8: Net-(J4-PadB8) -> (no net)
- J4 pad B9: Net-(J4-PadB9) -> (no net)
- J5 pad A1: Net-(J5-PadA1) -> (no net)
- J5 pad A10: Net-(J5-PadA10) -> (no net)
- J5 pad A11: Net-(J5-PadA11) -> (no net)
- J5 pad A12: Net-(J5-PadA12) -> (no net)
- J5 pad A13: Net-(J5-PadA13) -> (no net)
- J5 pad A14: Net-(J5-PadA14) -> (no net)
- J5 pad A15: Net-(J5-PadA15) -> (no net)
- J5 pad A16: Net-(J5-PadA16) -> (no net)
- J5 pad A17: Net-(J5-PadA17) -> (no net)
- J5 pad A18: Net-(J5-PadA18) -> (no net)
- J5 pad A2: Net-(J5-PadA2) -> (no net)
- J5 pad A3: Net-(J5-PadA3) -> (no net)
- J5 pad A4: Net-(J5-PadA4) -> (no net)
- J5 pad A5: Net-(J5-PadA5) -> (no net)
- J5 pad A6: Net-(J5-PadA6) -> (no net)
- J5 pad A7: Net-(J5-PadA7) -> (no net)
- J5 pad A8: Net-(J5-PadA8) -> (no net)
- J5 pad A9: Net-(J5-PadA9) -> (no net)
- J5 pad B1: Net-(J5-PadB1) -> (no net)
- J5 pad B10: Net-(J5-PadB10) -> (no net)
- J5 pad B11: Net-(J5-PadB11) -> (no net)
- J5 pad B12: Net-(J5-PadB12) -> (no net)
- J5 pad B13: Net-(J5-PadB13) -> (no net)
- J5 pad B14: Net-(J5-PadB14) -> (no net)
- J5 pad B15: Net-(J5-PadB15) -> (no net)
- J5 pad B16: Net-(J5-PadB16) -> (no net)
- J5 pad B17: Net-(J5-PadB17) -> (no net)
- J5 pad B18: Net-(J5-PadB18) -> (no net)
- J5 pad B2: Net-(J5-PadB2) -> (no net)
- J5 pad B3: Net-(J5-PadB3) -> (no net)
- J5 pad B4: Net-(J5-PadB4) -> (no net)
- J5 pad B5: Net-(J5-PadB5) -> (no net)
- J5 pad B6: Net-(J5-PadB6) -> (no net)
- J5 pad B7: Net-(J5-PadB7) -> (no net)
- J5 pad B8: Net-(J5-PadB8) -> (no net)
- J5 pad B9: Net-(J5-PadB9) -> (no net)
- J6 pad A1: Net-(J6-PadA1) -> (no net)
- J6 pad A10: Net-(J6-PadA10) -> (no net)
- J6 pad A11: Net-(J6-PadA11) -> (no net)
- J6 pad A12: Net-(J6-PadA12) -> (no net)
- J6 pad A13: Net-(J6-PadA13) -> (no net)
- J6 pad A14: Net-(J6-PadA14) -> (no net)
- J6 pad A15: Net-(J6-PadA15) -> (no net)
- J6 pad A16: Net-(J6-PadA16) -> (no net)
- J6 pad A17: Net-(J6-PadA17) -> (no net)
- J6 pad A18: Net-(J6-PadA18) -> (no net)
- J6 pad A2: Net-(J6-PadA2) -> (no net)
- J6 pad A3: Net-(J6-PadA3) -> (no net)
- J6 pad A4: Net-(J6-PadA4) -> (no net)
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
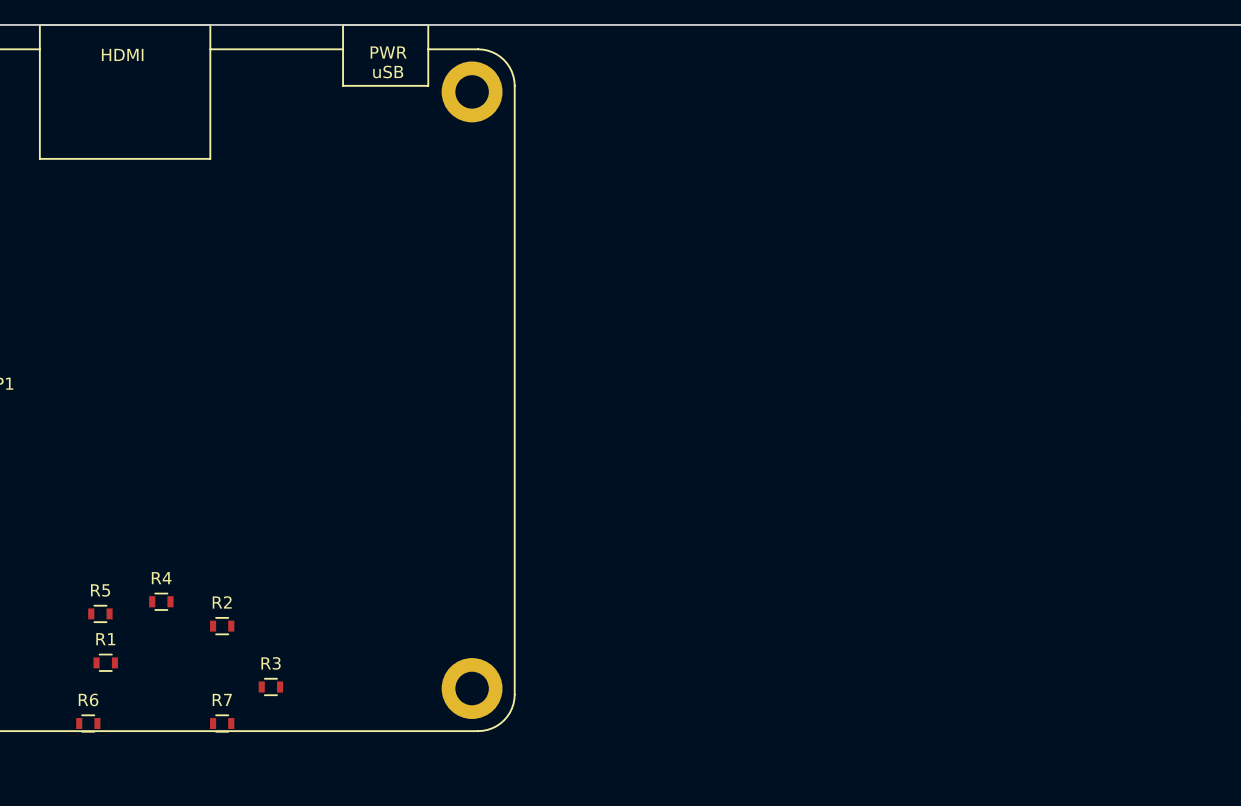
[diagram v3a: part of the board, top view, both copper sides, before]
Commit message: wip, added 3.3V reg
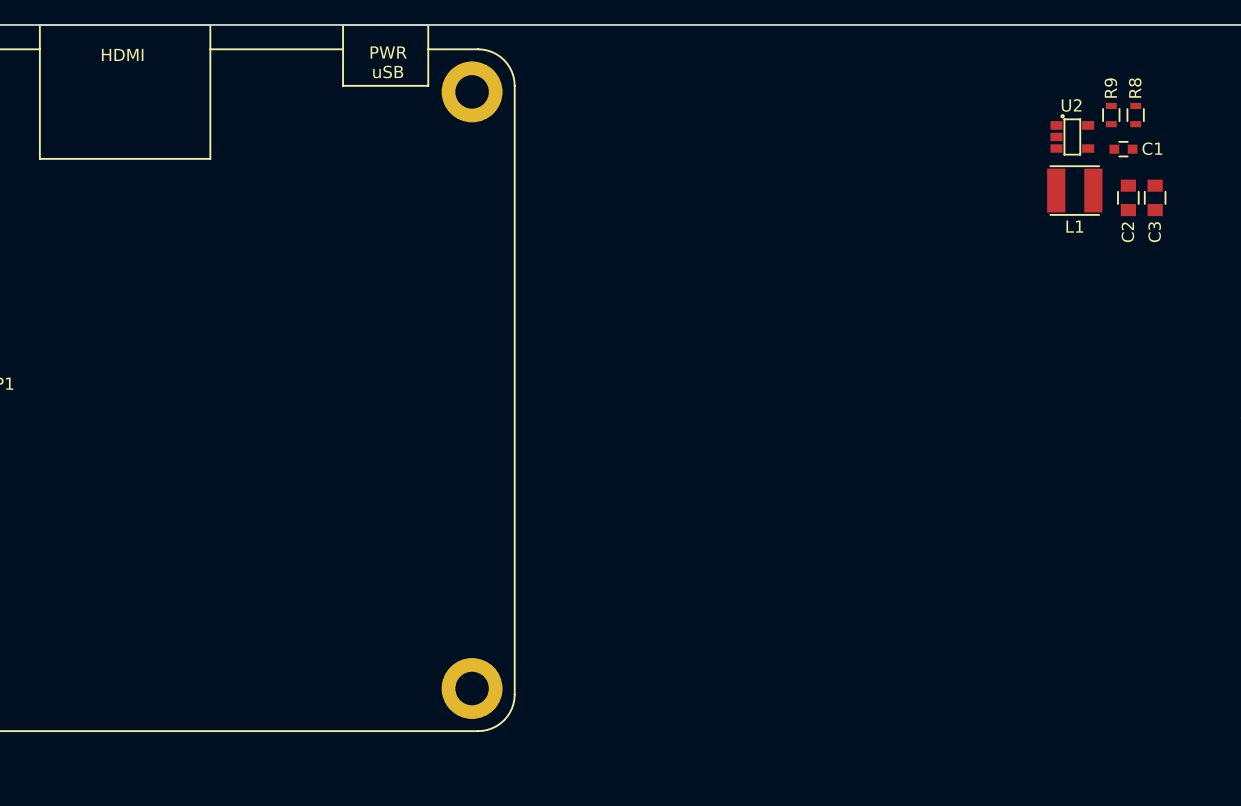
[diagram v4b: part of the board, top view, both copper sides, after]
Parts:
- removed R1, R2, R3, R4, R5, R6, R7: 10k, Resistors_SMD:R_0603
- added C1: 4.7uF, Capacitors_SMD:C_0603, F.Cu at (202.0, 48.2)
- added C2: 22uF, Capacitors_SMD:C_0805, F.Cu at (202.4, 52.2)
- added C3: 22uF, Capacitors_SMD:C_0805, F.Cu at (204.6, 52.2)
- added L1: INDUCTOR_SRN4026-2R2Y, Main:INDP400400X250, F.Cu at (198.0, 51.6)
- added R8: 27k, Resistors_SMD:R_0603, F.Cu at (203.0, 45.4)
- added R9: 6k, Resistors_SMD:R_0603, F.Cu at (201.0, 45.4)
- added U2: AP3418, Main:SOT095P300X150X145-5, F.Cu at (197.8, 47.2)
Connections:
- J15 pad 1: (no net) -> GND
- J15 pad 2: (no net) -> GND
- J15 pad 3: (no net) -> GND
- J15 pad 4: (no net) -> GND
- J15 pad 5: (no net) -> HT
- J15 pad 6: (no net) -> HT
- J15 pad 7: (no net) -> HT
- J15 pad 8: (no net) -> HT
- J16 pad 2: (no net) -> GND
- J16 pad 3: (no net) -> GND
- J16 pad 4: (no net) -> +5V
- J17 pad 1: (no net) -> HT
- J17 pad 2: (no net) -> GND
- J17 pad 3: (no net) -> GND
- J17 pad 4: (no net) -> HT
